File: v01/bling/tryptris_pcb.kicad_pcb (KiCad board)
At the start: 2 copper layers, 298.8 x 122 mm, 225 parts, among them J1 USB_C_Receptacle_USB2.0, J2 I2C-L, J3 I2C-R, SW1 Reset, U1 ATmega32U4-AU, U2 MCP23017_SO, U3 IS31FL3733-TQ, U4 HOLE, U4 IS31FL3733-TQ, Y1 16Mhz

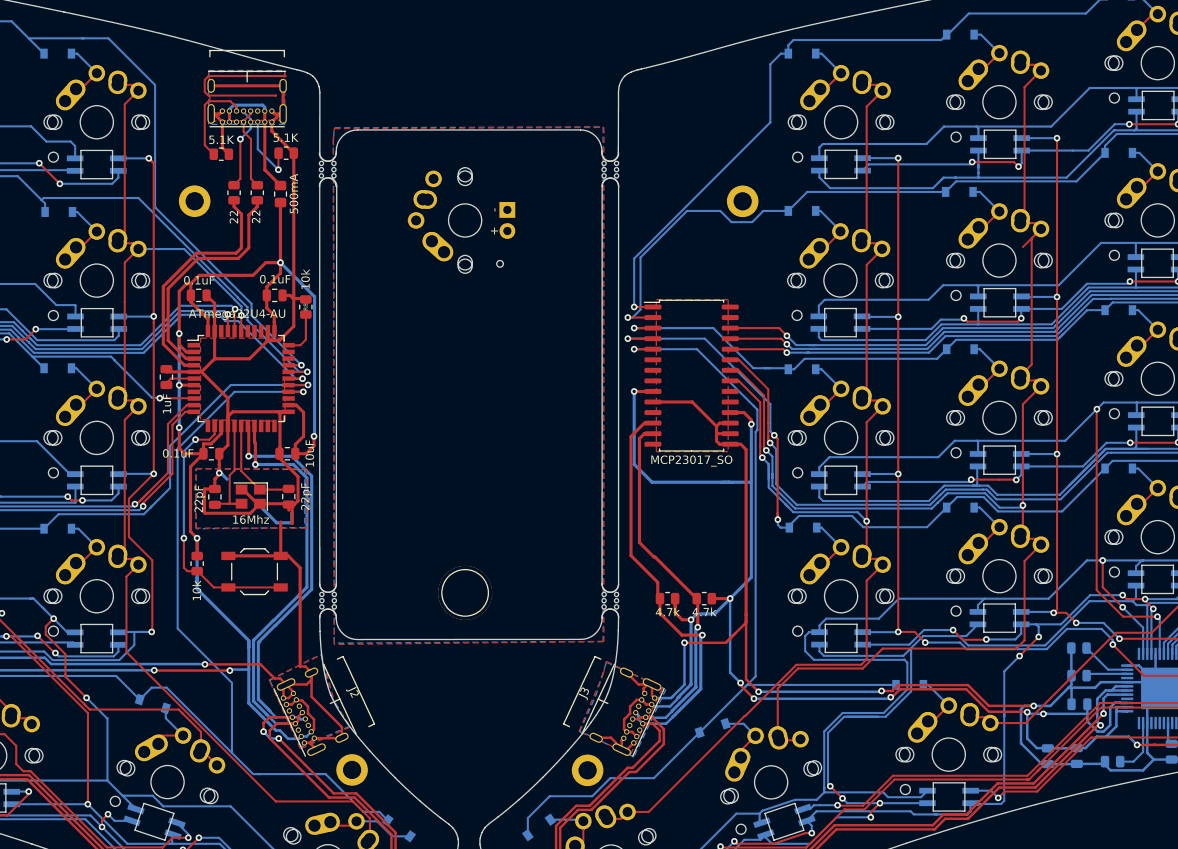
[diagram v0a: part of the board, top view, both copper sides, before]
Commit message: Use freeform routing to get USB ports in a better position.
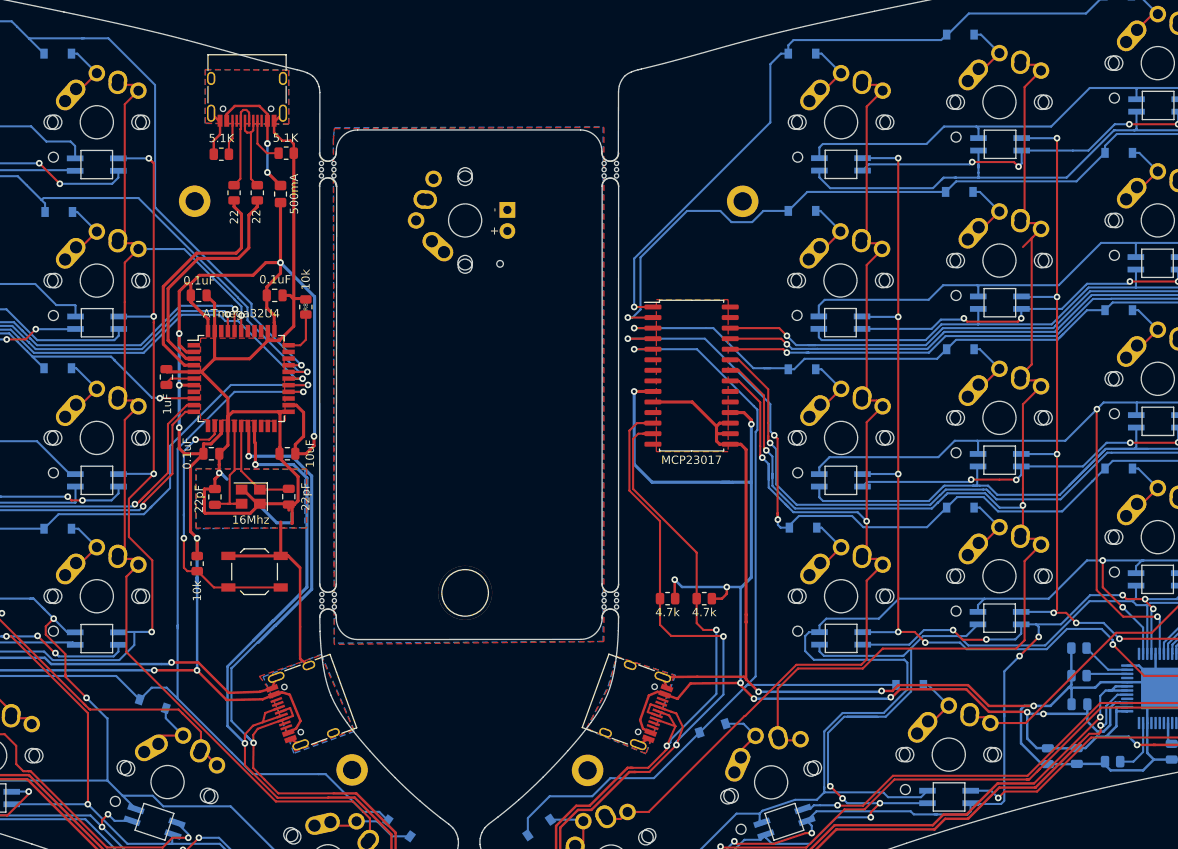
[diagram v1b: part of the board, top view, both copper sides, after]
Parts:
- J1, J2, J3: footprint Type-C:USB_C_GCT_USB4085 -> Connector_USB:USB_C_Receptacle_HRO_TYPE-C-31-M-12
- U1: value ATmega32U4-AU -> ATmega32U4
- U2: value MCP23017_SO -> MCP23017
- moved J3 3.36 mm to (194.9, 114.8), turned to 250 degrees
- moved J2 3.26 mm to (157.2, 114.8), turned to 110 degrees
- moved J1 1.90 mm to (149.3, 40.9)
- turned R3 to 180 degrees
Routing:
- net GND: track 325.9 -> 287.3 mm
- net VSS: track 211.3 -> 190.8 mm, vias 4 -> 3
- net (no net): track 20.2 -> 0.00 mm
- net SCL-R: track 165.4 -> 180.5 mm, vias 2 -> 3
- net SDA-R: track 156.1 -> 168.1 mm, vias 2 -> 3
- net +5V: track 263.4 -> 252.0 mm
- net Row4-L: track 124.1 -> 115.0 mm
- net SCL-L: track 174.3 -> 182.8 mm, vias 4 -> 3
- net SDA-L: track 164.2 -> 172.2 mm, vias 2 -> 3
- net Net-(J1-PadB5): track 11.1 -> 4.20 mm
- net VBUS: track 227.7 -> 223.0 mm
- net Net-(J1-PadA5): track 8.77 -> 5.81 mm, vias 1 -> 0
- net Net-(J1-PadA6): track 10.1 -> 11.3 mm, vias 1 -> 0
- net VCC: track 16.7 -> 16.2 mm, vias 0 -> 2

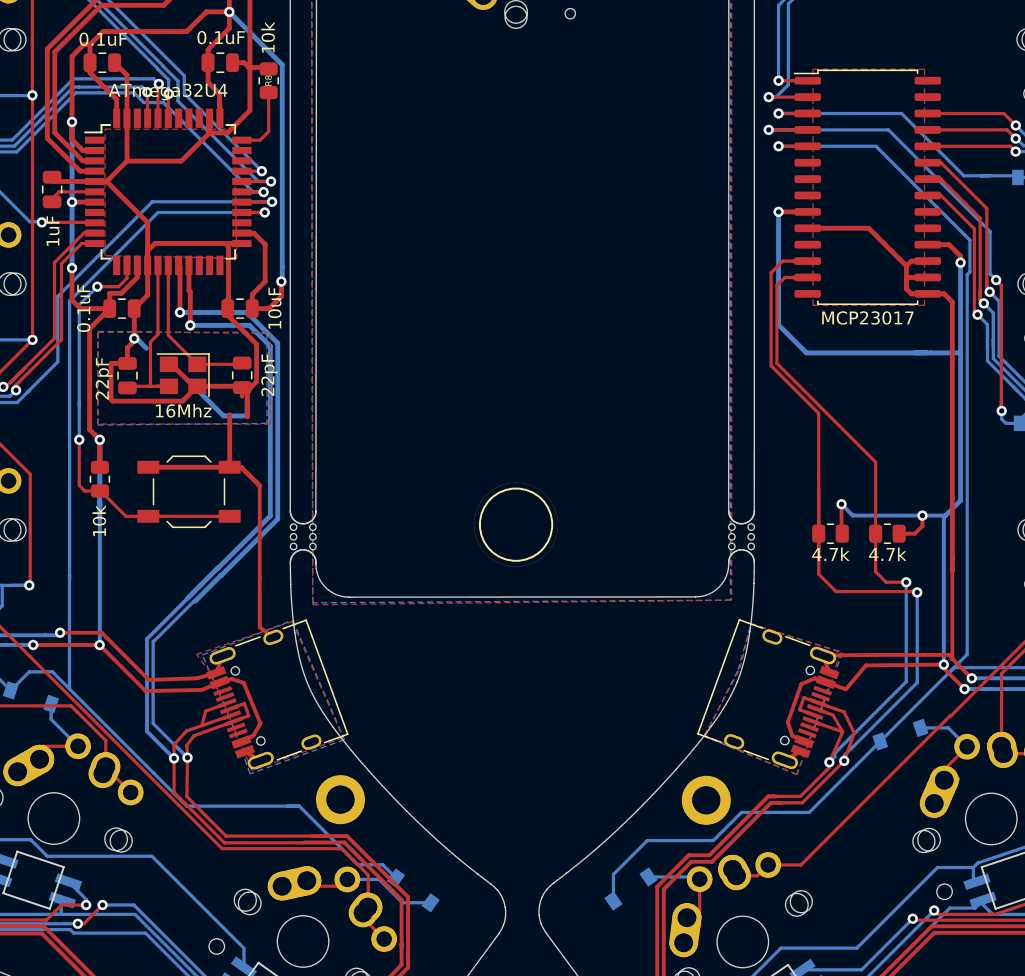
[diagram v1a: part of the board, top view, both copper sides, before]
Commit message: Move I2C resistors to the left side for bling
This should ensure that the LED drivers on the left side work correctly
when the right side is not plugged in.
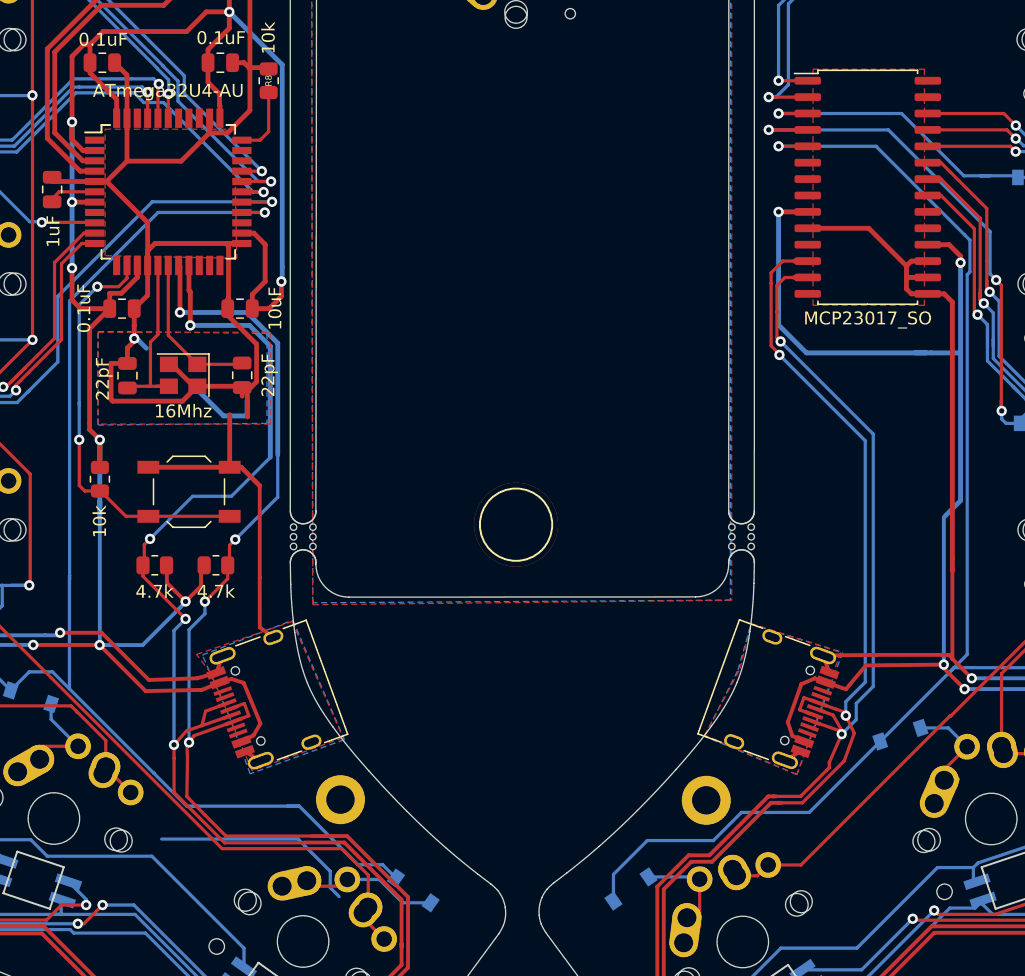
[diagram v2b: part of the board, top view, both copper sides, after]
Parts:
- U1: value ATmega32U4 -> ATmega32U4-AU
- U2: value MCP23017 -> MCP23017_SO
- moved R6 52.4 mm to (147.5, 104.8)
- moved R7 52.1 mm to (152.2, 104.8)
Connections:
- R6 pad 1: SCL-R -> SDA-L
- R6 pad 2: VBUS -> +5V
- R7 pad 1: SDA-R -> +5V
- R7 pad 2: VBUS -> SCL-L
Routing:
- net SCL-R: track 180.5 -> 163.9 mm
- net (no net): track 0.00 -> 16.3 mm
- net +5V: track 252.0 -> 267.2 mm, vias 10 -> 11
- net VBUS: track 223.0 -> 209.4 mm, vias 13 -> 11
- net SDA-R: track 168.1 -> 162.3 mm
- net SCL-L: track 182.8 -> 177.4 mm, vias 3 -> 5
- net SDA-L: track 172.2 -> 173.8 mm, vias 3 -> 5

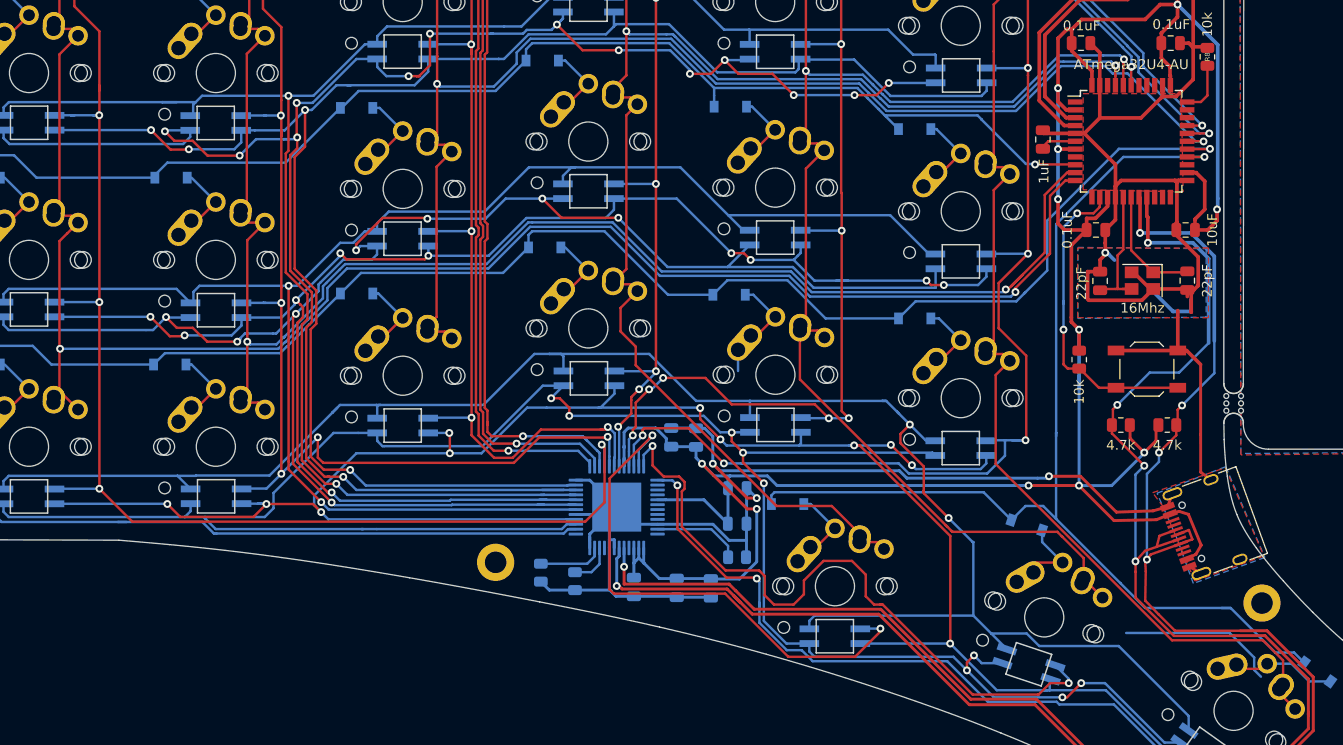
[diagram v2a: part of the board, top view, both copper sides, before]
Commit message: Add ISP port to the bling board.
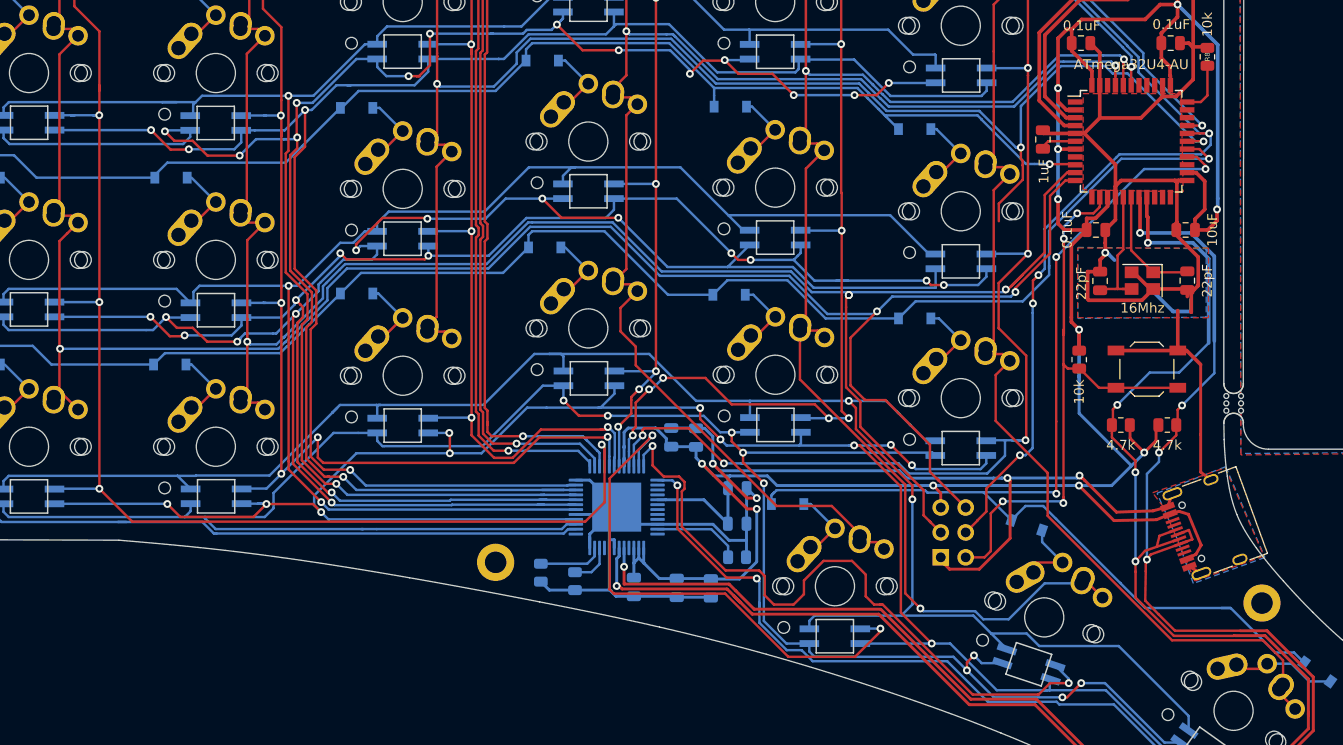
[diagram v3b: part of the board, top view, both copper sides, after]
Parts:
- added J4: AVR-ISP-6, random-keyboard-parts:Reset_Pretty-Mask, B.Cu at (130.4, 115.8)
- U3, U4: value IS31FL3733-TQ -> IS31FL3733
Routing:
- net Row1-L: track 151.6 -> 207.9 mm, vias 1 -> 4
- net Net-(J4-Pad5): track 33.0 -> 62.1 mm, vias 2 -> 4
- net Col0: track 189.0 -> 218.1 mm, vias 2 -> 3
- net Col1: track 172.6 -> 201.6 mm, vias 2 -> 4
- net (no net): track 16.3 -> 0.00 mm
- net GND: track 287.3 -> 302.7 mm, vias 4 -> 5
- net Col2: track 160.2 -> 174.3 mm, vias 2 -> 3
- net Col4: track 153.7 -> 161.8 mm, vias 2 -> 3
- net Row4-L: track 115.0 -> 118.6 mm, vias 1 -> 3
- net +5V: track 267.2 -> 270.6 mm
- net Left-SW2: track 225.4 -> 223.3 mm
- net Net-(D23-Pad2): track 9.77 -> 7.61 mm
- net Left-SW1: track 250.7 -> 252.5 mm
- net SDA-L: track 173.8 -> 172.8 mm
- net Left-SW3: track 216.3 -> 215.5 mm
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
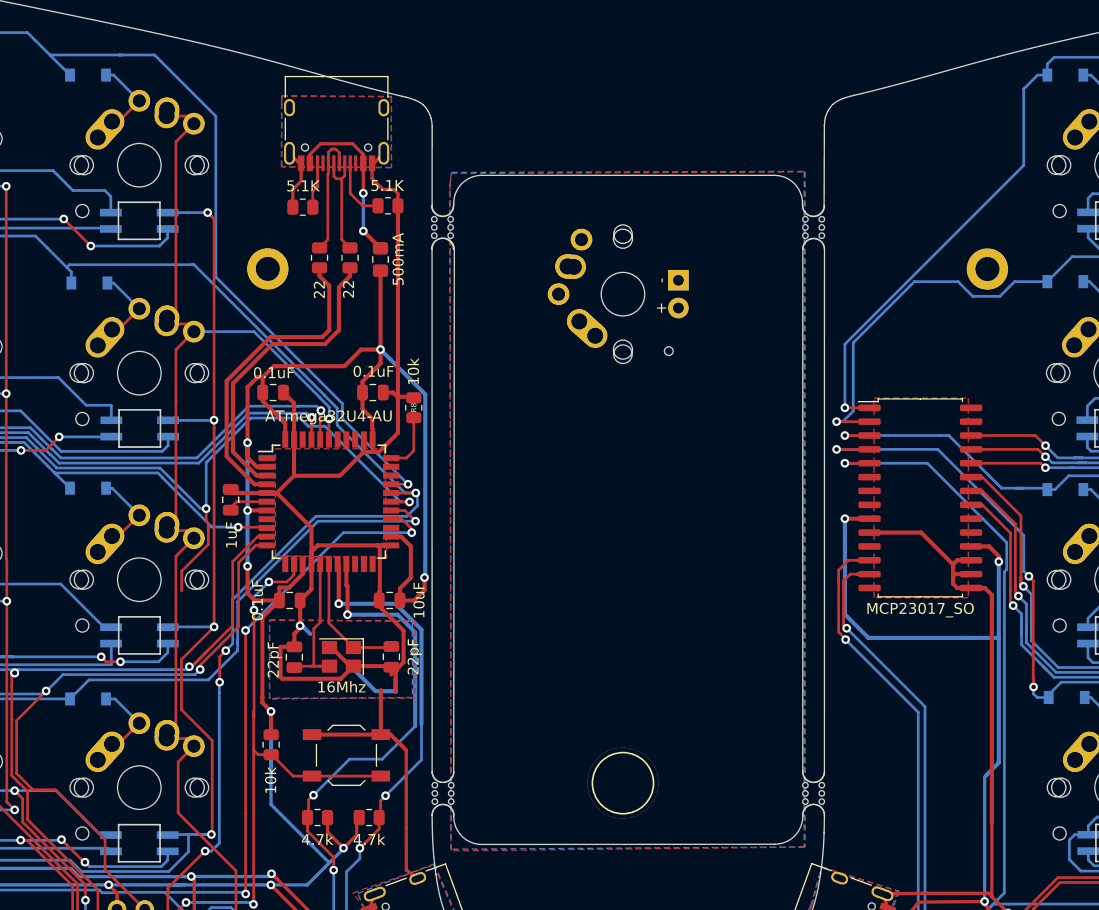
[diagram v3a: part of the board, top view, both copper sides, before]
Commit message: Fix ISP connection and move mounting holes
I had the pins wrong. Top mounting holes are more equal in height and
evenly spread around the board.
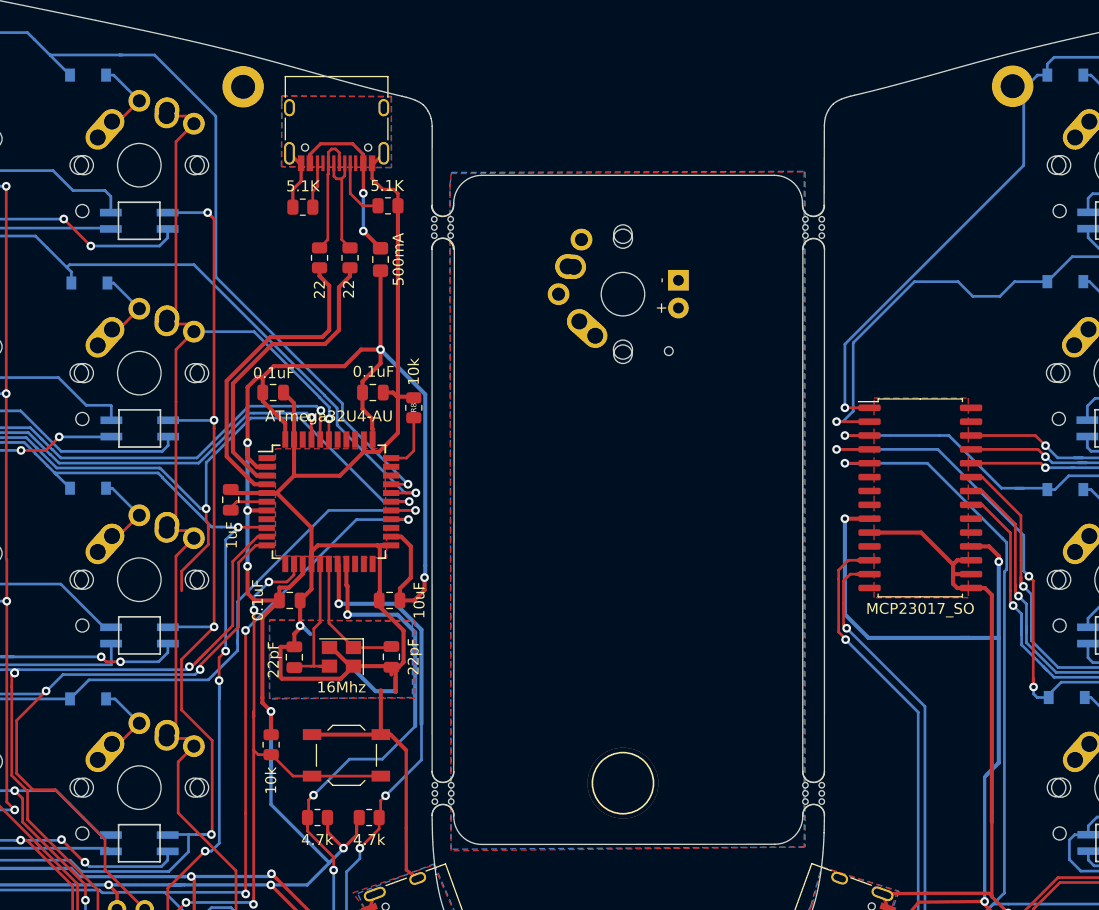
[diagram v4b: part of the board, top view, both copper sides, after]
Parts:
- removed the REF** at (208.9, 54.6)
- removed the REF** at (143.0, 54.6)
- added REF**: MountingHole_2.2mm_M2_DIN965_Pad, MountingHole:MountingHole_2.2mm_M2_DIN965_Pad, F.Cu at (211.2, 37.9)
- added REF**: MountingHole_2.2mm_M2_DIN965_Pad, MountingHole:MountingHole_2.2mm_M2_DIN965_Pad, F.Cu at (140.7, 37.9)
- U3, U4: value IS31FL3733 -> IS31FL3733-TQ
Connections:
- J4 pad 3: Row1-L -> Row2-L
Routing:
- net Row1-L: track 207.9 -> 151.6 mm, vias 4 -> 1
- net Row2-L: track 129.8 -> 172.8 mm, vias 1 -> 4
- net Row4-L: track 118.6 -> 117.8 mm
